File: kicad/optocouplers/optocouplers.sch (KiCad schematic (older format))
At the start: 112 parts, among them Q1 PN2222A, Q2 PN2222A, Q3 PN2222A, Q4 PN2222A, Q5 PN2222A, Q6 PN2222A, Q7 PN2222A, Q8 PN2222A

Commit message: update kicad drawings for optocouplers
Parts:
- added J1: Conn_02x13_Top_Bottom, symbol Conn_02x13_Top_Bottom
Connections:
- no-connect marks 0 -> 8

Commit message: Update to the latest version of optocoupler pcb design
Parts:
- J1: footprint (none) -> Connectors_Multicomp:Multicomp_MC9A12-2634_2x13x2.54mm_Straight; symbol Conn_02x13_Top_Bottom -> optocouplers-rescue:Conn_02x13_Top_Bottom
- Q1, Q2, Q3, Q4, Q5, Q6, Q7, Q8: symbol PN2222A -> optocouplers-rescue:PN2222A
- R1, R2, R3, R4, R5, R6, R7, R8, R_A0, R_A1, R_A10, R_A11, R_A2, R_A3, R_A4, R_A5, R_A6, R_A7, R_A8, R_A9, R_B0, R_B1, R_B10, R_B11, R_B12, R_B2, R_B3, R_B4, R_B5, R_B6, R_B7, R_B8, R_B9, R_C0, R_C1, R_C10, R_C11, R_C2, R_C3, R_C4, R_C5, R_C6, R_C7, R_C8, R_C9, R_D0, R_D1, R_D10, R_D2, R_D3, R_D4, R_D5, R_D6, R_D7, R_D8, R_D9: symbol R -> optocouplers-rescue:R
- U_A0, U_A1, U_A10, U_A11, U_A2, U_A3, U_A4, U_A5, U_A6, U_A7, U_A8, U_A9, U_B0, U_B1, U_B10, U_B11, U_B12, U_B2, U_B3, U_B4, U_B5, U_B6, U_B7, U_B8, U_B9, U_C0, U_C1, U_C10, U_C11, U_C2, U_C3, U_C4, U_C5, U_C6, U_C7, U_C8, U_C9, U_D0, U_D1, U_D10, U_D2, U_D3, U_D4, U_D5, U_D6, U_D7, U_D8, U_D9: symbol ITR9608 -> optocouplers-rescue:ITR9608
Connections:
- wire segments 56 -> 96

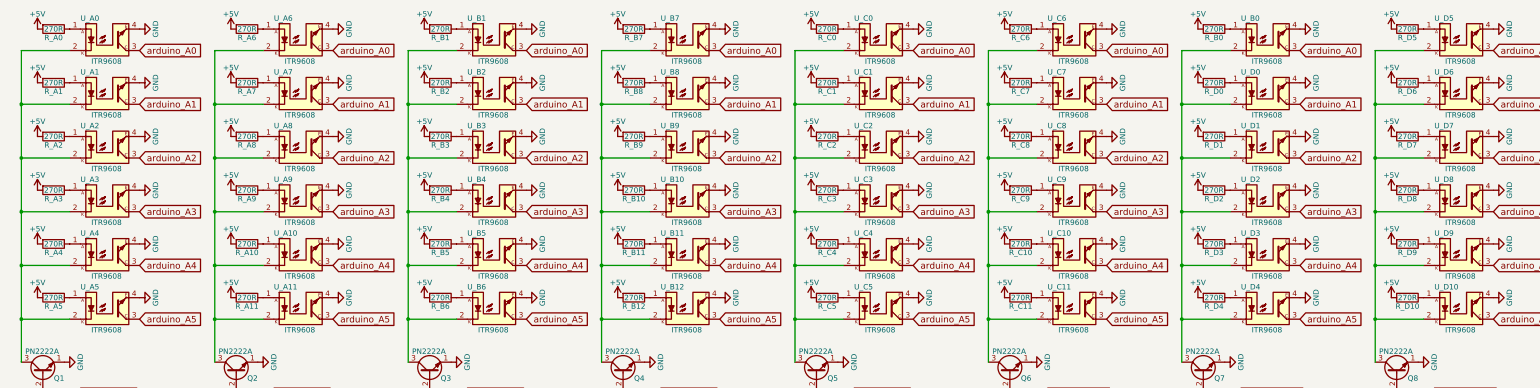
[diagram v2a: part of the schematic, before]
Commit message: Slightly change wiring of optocouplers
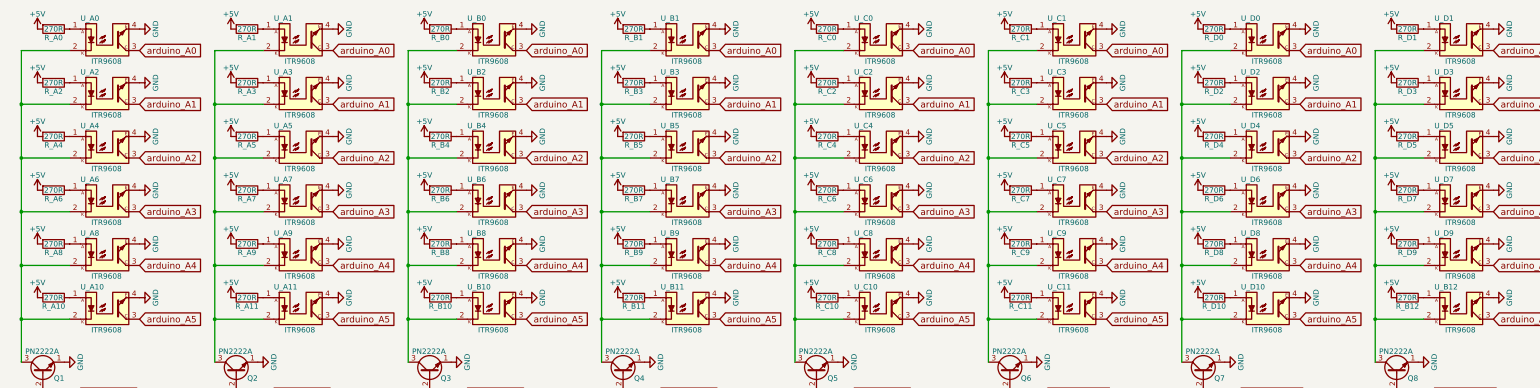
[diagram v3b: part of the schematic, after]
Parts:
- R1, R2, R3, R4, R5, R6, R7, R8, R_A0, R_A11, R_B2, R_C0, R_C11, R_D9: footprint Resistors_ThroughHole:R_Axial_DIN0207_L6.3mm_D2.5mm_P10.16mm_Horizontal -> Resistor_SMD:R_1206_3216Metric_Pad1.42x1.75mm_HandSolder
- R_A1: renamed from R_A6; footprint Resistors_ThroughHole:R_Axial_DIN0207_L6.3mm_D2.5mm_P10.16mm_Horizontal -> Resistor_SMD:R_1206_3216Metric_Pad1.42x1.75mm_HandSolder
- R_A10: renamed from R_A5; footprint Resistors_ThroughHole:R_Axial_DIN0207_L6.3mm_D2.5mm_P10.16mm_Horizontal -> Resistor_SMD:R_1206_3216Metric_Pad1.42x1.75mm_HandSolder
- R_A2: renamed from R_A1; footprint Resistors_ThroughHole:R_Axial_DIN0207_L6.3mm_D2.5mm_P10.16mm_Horizontal -> Resistor_SMD:R_1206_3216Metric_Pad1.42x1.75mm_HandSolder
- R_A3: renamed from R_A7; footprint Resistors_ThroughHole:R_Axial_DIN0207_L6.3mm_D2.5mm_P10.16mm_Horizontal -> Resistor_SMD:R_1206_3216Metric_Pad1.42x1.75mm_HandSolder
- R_A4: renamed from R_A2; footprint Resistors_ThroughHole:R_Axial_DIN0207_L6.3mm_D2.5mm_P10.16mm_Horizontal -> Resistor_SMD:R_1206_3216Metric_Pad1.42x1.75mm_HandSolder
- R_A5: renamed from R_A8; footprint Resistors_ThroughHole:R_Axial_DIN0207_L6.3mm_D2.5mm_P10.16mm_Horizontal -> Resistor_SMD:R_1206_3216Metric_Pad1.42x1.75mm_HandSolder
- R_A6: renamed from R_A3; footprint Resistors_ThroughHole:R_Axial_DIN0207_L6.3mm_D2.5mm_P10.16mm_Horizontal -> Resistor_SMD:R_1206_3216Metric_Pad1.42x1.75mm_HandSolder
- R_A7: renamed from R_A9; footprint Resistors_ThroughHole:R_Axial_DIN0207_L6.3mm_D2.5mm_P10.16mm_Horizontal -> Resistor_SMD:R_1206_3216Metric_Pad1.42x1.75mm_HandSolder
- R_A8: renamed from R_A4; footprint Resistors_ThroughHole:R_Axial_DIN0207_L6.3mm_D2.5mm_P10.16mm_Horizontal -> Resistor_SMD:R_1206_3216Metric_Pad1.42x1.75mm_HandSolder
- R_A9: renamed from R_A10; footprint Resistors_ThroughHole:R_Axial_DIN0207_L6.3mm_D2.5mm_P10.16mm_Horizontal -> Resistor_SMD:R_1206_3216Metric_Pad1.42x1.75mm_HandSolder
- R_B0: renamed from R_B1; footprint Resistors_ThroughHole:R_Axial_DIN0207_L6.3mm_D2.5mm_P10.16mm_Horizontal -> Resistor_SMD:R_1206_3216Metric_Pad1.42x1.75mm_HandSolder
- R_B1: renamed from R_B7; footprint Resistors_ThroughHole:R_Axial_DIN0207_L6.3mm_D2.5mm_P10.16mm_Horizontal -> Resistor_SMD:R_1206_3216Metric_Pad1.42x1.75mm_HandSolder
- R_B10: renamed from R_B6; footprint Resistors_ThroughHole:R_Axial_DIN0207_L6.3mm_D2.5mm_P10.16mm_Horizontal -> Resistor_SMD:R_1206_3216Metric_Pad1.42x1.75mm_HandSolder
- R_B11: renamed from R_B12; footprint Resistors_ThroughHole:R_Axial_DIN0207_L6.3mm_D2.5mm_P10.16mm_Horizontal -> Resistor_SMD:R_1206_3216Metric_Pad1.42x1.75mm_HandSolder
- R_B12: renamed from R_D10; footprint Resistors_ThroughHole:R_Axial_DIN0207_L6.3mm_D2.5mm_P10.16mm_Horizontal -> Resistor_SMD:R_1206_3216Metric_Pad1.42x1.75mm_HandSolder
- R_B3: renamed from R_B8; footprint Resistors_ThroughHole:R_Axial_DIN0207_L6.3mm_D2.5mm_P10.16mm_Horizontal -> Resistor_SMD:R_1206_3216Metric_Pad1.42x1.75mm_HandSolder
- R_B4: renamed from R_B3; footprint Resistors_ThroughHole:R_Axial_DIN0207_L6.3mm_D2.5mm_P10.16mm_Horizontal -> Resistor_SMD:R_1206_3216Metric_Pad1.42x1.75mm_HandSolder
- R_B5: renamed from R_B9; footprint Resistors_ThroughHole:R_Axial_DIN0207_L6.3mm_D2.5mm_P10.16mm_Horizontal -> Resistor_SMD:R_1206_3216Metric_Pad1.42x1.75mm_HandSolder
- R_B6: renamed from R_B4; footprint Resistors_ThroughHole:R_Axial_DIN0207_L6.3mm_D2.5mm_P10.16mm_Horizontal -> Resistor_SMD:R_1206_3216Metric_Pad1.42x1.75mm_HandSolder
- R_B7: renamed from R_B10; footprint Resistors_ThroughHole:R_Axial_DIN0207_L6.3mm_D2.5mm_P10.16mm_Horizontal -> Resistor_SMD:R_1206_3216Metric_Pad1.42x1.75mm_HandSolder
- R_B8: renamed from R_B5; footprint Resistors_ThroughHole:R_Axial_DIN0207_L6.3mm_D2.5mm_P10.16mm_Horizontal -> Resistor_SMD:R_1206_3216Metric_Pad1.42x1.75mm_HandSolder
- R_B9: renamed from R_B11; footprint Resistors_ThroughHole:R_Axial_DIN0207_L6.3mm_D2.5mm_P10.16mm_Horizontal -> Resistor_SMD:R_1206_3216Metric_Pad1.42x1.75mm_HandSolder
- R_C1: renamed from R_C6; footprint Resistors_ThroughHole:R_Axial_DIN0207_L6.3mm_D2.5mm_P10.16mm_Horizontal -> Resistor_SMD:R_1206_3216Metric_Pad1.42x1.75mm_HandSolder
- R_C10: renamed from R_C5; footprint Resistors_ThroughHole:R_Axial_DIN0207_L6.3mm_D2.5mm_P10.16mm_Horizontal -> Resistor_SMD:R_1206_3216Metric_Pad1.42x1.75mm_HandSolder
- R_C2: renamed from R_C1; footprint Resistors_ThroughHole:R_Axial_DIN0207_L6.3mm_D2.5mm_P10.16mm_Horizontal -> Resistor_SMD:R_1206_3216Metric_Pad1.42x1.75mm_HandSolder
- R_C3: renamed from R_C7; footprint Resistors_ThroughHole:R_Axial_DIN0207_L6.3mm_D2.5mm_P10.16mm_Horizontal -> Resistor_SMD:R_1206_3216Metric_Pad1.42x1.75mm_HandSolder
- R_C4: renamed from R_C2; footprint Resistors_ThroughHole:R_Axial_DIN0207_L6.3mm_D2.5mm_P10.16mm_Horizontal -> Resistor_SMD:R_1206_3216Metric_Pad1.42x1.75mm_HandSolder
- R_C5: renamed from R_C8; footprint Resistors_ThroughHole:R_Axial_DIN0207_L6.3mm_D2.5mm_P10.16mm_Horizontal -> Resistor_SMD:R_1206_3216Metric_Pad1.42x1.75mm_HandSolder
- R_C6: renamed from R_C3; footprint Resistors_ThroughHole:R_Axial_DIN0207_L6.3mm_D2.5mm_P10.16mm_Horizontal -> Resistor_SMD:R_1206_3216Metric_Pad1.42x1.75mm_HandSolder
- R_C7: renamed from R_C9; footprint Resistors_ThroughHole:R_Axial_DIN0207_L6.3mm_D2.5mm_P10.16mm_Horizontal -> Resistor_SMD:R_1206_3216Metric_Pad1.42x1.75mm_HandSolder
- R_C8: renamed from R_C4; footprint Resistors_ThroughHole:R_Axial_DIN0207_L6.3mm_D2.5mm_P10.16mm_Horizontal -> Resistor_SMD:R_1206_3216Metric_Pad1.42x1.75mm_HandSolder
- R_C9: renamed from R_C10; footprint Resistors_ThroughHole:R_Axial_DIN0207_L6.3mm_D2.5mm_P10.16mm_Horizontal -> Resistor_SMD:R_1206_3216Metric_Pad1.42x1.75mm_HandSolder
- R_D0: renamed from R_B0; footprint Resistors_ThroughHole:R_Axial_DIN0207_L6.3mm_D2.5mm_P10.16mm_Horizontal -> Resistor_SMD:R_1206_3216Metric_Pad1.42x1.75mm_HandSolder
- R_D1: renamed from R_D5; footprint Resistors_ThroughHole:R_Axial_DIN0207_L6.3mm_D2.5mm_P10.16mm_Horizontal -> Resistor_SMD:R_1206_3216Metric_Pad1.42x1.75mm_HandSolder
- R_D10: renamed from R_D4; footprint Resistors_ThroughHole:R_Axial_DIN0207_L6.3mm_D2.5mm_P10.16mm_Horizontal -> Resistor_SMD:R_1206_3216Metric_Pad1.42x1.75mm_HandSolder
- R_D2: renamed from R_D0; footprint Resistors_ThroughHole:R_Axial_DIN0207_L6.3mm_D2.5mm_P10.16mm_Horizontal -> Resistor_SMD:R_1206_3216Metric_Pad1.42x1.75mm_HandSolder
- R_D3: renamed from R_D6; footprint Resistors_ThroughHole:R_Axial_DIN0207_L6.3mm_D2.5mm_P10.16mm_Horizontal -> Resistor_SMD:R_1206_3216Metric_Pad1.42x1.75mm_HandSolder
- R_D4: renamed from R_D1; footprint Resistors_ThroughHole:R_Axial_DIN0207_L6.3mm_D2.5mm_P10.16mm_Horizontal -> Resistor_SMD:R_1206_3216Metric_Pad1.42x1.75mm_HandSolder
- R_D5: renamed from R_D7; footprint Resistors_ThroughHole:R_Axial_DIN0207_L6.3mm_D2.5mm_P10.16mm_Horizontal -> Resistor_SMD:R_1206_3216Metric_Pad1.42x1.75mm_HandSolder
- R_D6: renamed from R_D2; footprint Resistors_ThroughHole:R_Axial_DIN0207_L6.3mm_D2.5mm_P10.16mm_Horizontal -> Resistor_SMD:R_1206_3216Metric_Pad1.42x1.75mm_HandSolder
- R_D7: renamed from R_D8; footprint Resistors_ThroughHole:R_Axial_DIN0207_L6.3mm_D2.5mm_P10.16mm_Horizontal -> Resistor_SMD:R_1206_3216Metric_Pad1.42x1.75mm_HandSolder
- R_D8: renamed from R_D3; footprint Resistors_ThroughHole:R_Axial_DIN0207_L6.3mm_D2.5mm_P10.16mm_Horizontal -> Resistor_SMD:R_1206_3216Metric_Pad1.42x1.75mm_HandSolder
- renumbered U_A6 to U_A1, U_A5 to U_A10, U_A1 to U_A2, U_A7 to U_A3, U_A2 to U_A4, U_A8 to U_A5, U_A3 to U_A6, U_A9 to U_A7, U_A4 to U_A8, U_A10 to U_A9, U_B1 to U_B0, U_B7 to U_B1, U_B6 to U_B10, U_B12 to U_B11, U_D10 to U_B12, U_B8 to U_B3, U_B3 to U_B4, U_B9 to U_B5, U_B4 to U_B6, U_B10 to U_B7, U_B5 to U_B8, U_B11 to U_B9, U_C6 to U_C1, U_C5 to U_C10, U_C1 to U_C2, U_C7 to U_C3, U_C2 to U_C4, U_C8 to U_C5, U_C3 to U_C6, U_C9 to U_C7, U_C4 to U_C8, U_C10 to U_C9, U_B0 to U_D0, U_D5 to U_D1, U_D4 to U_D10, U_D0 to U_D2, U_D6 to U_D3, U_D1 to U_D4, U_D7 to U_D5, U_D2 to U_D6, U_D8 to U_D7, U_D3 to U_D8

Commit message: almost complete pcb
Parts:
- removed J1: Conn_02x13_Top_Bottom, Connectors_Multicomp:Multicomp_MC9A12-2634_2x13x2.54mm_Straight, symbol optocouplers-rescue:Conn_02x13_Top_Bottom
- added Conn1: Conn_02x13_Odd_Even, Connector_Multicomp:Multicomp_MC9A12-2634_2x13_P2.54mm_Vertical, symbol Connector_Generic:Conn_02x13_Odd_Even
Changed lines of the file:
@@
-$EndComp
-$Comp
-L optocouplers-rescue:Conn_02x13_Top_Bottom J1
-U 1 1 5A4545DE
-P 2900 5600
-F 0 "J1" H 2950 6417 50  0000 C CNN
-F 1 "Conn_02x13_Top_Bottom" H 2950 6326 50  0000 C CNN
-F 2 "Connectors_Multicomp:Multicomp_MC9A12-2634_2x13x2.54mm_Straight" H 2900 5600 50  0001 C CNN
-F 3 "~" H 2900 5600 50  0001 C CNN
-	1    2900 5600
-	1    0    0    -1
 $EndComp
 $Comp
@@
 L optocouplers-rescue:GND #PWR0109
 U 1 1 5A4568BF
-P 3200 5100
-F 0 "#PWR0109" H 3200 4850 50  0001 C CNN
-F 1 "GND" V 3205 4972 50  0000 R CNN
-F 2 "" H 3200 5100 50  0001 C CNN
-F 3 "" H 3200 5100 50  0001 C CNN
-	1    3200 5100
+P 3200 6200
+F 0 "#PWR0109" H 3200 5950 50  0001 C CNN
+F 1 "GND" V 3205 6072 50  0000 R CNN
+F 2 "" H 3200 6200 50  0001 C CNN
+F 3 "" H 3200 6200 50  0001 C CNN
+	1    3200 6200
 	0    -1   -1   0
 $EndComp
@@
 L optocouplers-rescue:GND #PWR0110
 U 1 1 5A456B8E
-P 2700 5100
-F 0 "#PWR0110" H 2700 4850 50  0001 C CNN
-F 1 "GND" V 2705 4972 50  0000 R CNN
-F 2 "" H 2700 5100 50  0001 C CNN
-F 3 "" H 2700 5100 50  0001 C CNN
-	1    2700 5100
+P 2700 6200
+F 0 "#PWR0110" H 2700 5950 50  0001 C CNN
+F 1 "GND" V 2705 6072 50  0000 R CNN
+F 2 "" H 2700 6200 50  0001 C CNN
+F 3 "" H 2700 6200 50  0001 C CNN
+	1    2700 6200
 	0    1    1    0
 $EndComp
-Text GLabel 2700 6200 0    60   Input ~ 0
+Text GLabel 2700 5800 0    60   Input ~ 0
 arduino_D12
-Text GLabel 2700 6100 0    60   Input ~ 0
+Text GLabel 2700 5700 0    60   Input ~ 0
 arduino_D11
-Text GLabel 2700 6000 0    60   Input ~ 0
+Text GLabel 2700 5600 0    60   Input ~ 0
 arduino_D10
-Text GLabel 2700 5900 0    60   Input ~ 0
+Text GLabel 2700 5500 0    60   Input ~ 0
 arduino_D9
-Text GLabel 2700 5800 0    60   Input ~ 0
+Text GLabel 2700 5400 0    60   Input ~ 0
 arduino_D8
-Text GLabel 2700 5700 0    60   Input ~ 0
+Text GLabel 2700 5300 0    60   Input ~ 0
 arduino_D7
-Text GLabel 2700 5600 0    60   Input ~ 0
+Text GLabel 2700 5200 0    60   Input ~ 0
 arduino_D6
-Text GLabel 2700 5500 0    60   Input ~ 0
+Text GLabel 2700 5100 0    60   Input ~ 0
 arduino_D5
-NoConn ~ 2700 5400
-NoConn ~ 2700 5300
-NoConn ~ 2700 5200
+Text GLabel 3200 5100 2    60   Input ~ 0
+arduino_A5
+Text GLabel 3200 5200 2    60   Input ~ 0
+arduino_A4
+Text GLabel 3200 5300 2    60   Input ~ 0
+arduino_A3
 Text GLabel 3200 5400 2    60   Input ~ 0
-arduino_A5
+arduino_A2
 Text GLabel 3200 5500 2    60   Input ~ 0
-arduino_A4
+arduino_A1
 Text GLabel 3200 5600 2    60   Input ~ 0
-arduino_A3
-Text GLabel 3200 5700 2    60   Input ~ 0
-arduino_A2
-Text GLabel 3200 5800 2    60   Input ~ 0
-arduino_A1
-Text GLabel 3200 5900 2    60   Input ~ 0
 arduino_A0
-NoConn ~ 3200 6200
 NoConn ~ 3200 6100
 NoConn ~ 3200 6000
-NoConn ~ 3200 5300
-NoConn ~ 3200 5200
 Wire Wire Line
 	900  2200 900  2700
@@
 Wire Wire Line
 	900  1700 900  2200
+NoConn ~ 2700 5900
+NoConn ~ 2700 6000
+NoConn ~ 2700 6100
+NoConn ~ 3200 5700
+NoConn ~ 3200 5800
+NoConn ~ 3200 5900
+$Comp
+L Connector_Generic:Conn_02x13_Odd_Even Conn1
+U 1 1 5D7EB063
+P 2900 5600
+F 0 "Conn1" H 2950 6417 50  0000 C CNN
+F 1 "Conn_02x13_Odd_Even" H 2950 6326 50  0000 C CNN
+F 2 "Connector_Multicomp:Multicomp_MC9A12-2634_2x13_P2.54mm_Vertical" H 2900 5600 50  0001 C CNN
+F 3 "~" H 2900 5600 50  0001 C CNN
+	1    2900 5600
+	1    0    0    -1
+$EndComp
 $EndSCHEMATC

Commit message: Add missing 2k resistors, change connectors (opto)
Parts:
- added R_R0, R_R1, R_R2, R_R3, R_R4, R_R5: 2k, symbol Device:R
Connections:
- net +5V: now also R_R0.2, R_R1.2, R_R2.2, R_R3.2, R_R4.2, R_R5.2
- net arduino_A0: now also R_R0.1
- net arduino_A1: now also R_R1.1
- net arduino_A2: now also R_R2.1
- net arduino_A3: now also R_R3.1
- net arduino_A4: now also R_R4.1
- net arduino_A5: now also R_R5.1
- net arduino_D10: now also Conn1.19 (Pin_19); no longer Conn1.13 (Pin_13)
- net arduino_D11: now also Conn1.21 (Pin_21); no longer Conn1.15 (Pin_15)
- net arduino_D12: now also Conn1.23 (Pin_23); no longer Conn1.17 (Pin_17)
- net arduino_D5: now also Conn1.9 (Pin_9); no longer Conn1.3 (Pin_3)
- net arduino_D6: now also Conn1.11 (Pin_11); no longer Conn1.5 (Pin_5)
- net arduino_D7: now also Conn1.13 (Pin_13); no longer Conn1.7 (Pin_7)
- net arduino_D8: now also Conn1.15 (Pin_15); no longer Conn1.9 (Pin_9)
- net arduino_D9: now also Conn1.17 (Pin_17); no longer Conn1.11 (Pin_11)
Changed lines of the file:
@@
 EESchema Schematic File Version 4
 LIBS:optocouplers-cache
-EELAYER 26 0
+EELAYER 30 0
 EELAYER END
 $Descr User 17717 7087
@@
 	0    1    1    0
 $EndComp
+Text GLabel 2700 6100 0    60   Input ~ 0
+arduino_D12
+Text GLabel 2700 6000 0    60   Input ~ 0
+arduino_D11
+Text GLabel 2700 5900 0    60   Input ~ 0
+arduino_D10
 Text GLabel 2700 5800 0    60   Input ~ 0
-arduino_D12
+arduino_D9
 Text GLabel 2700 5700 0    60   Input ~ 0
-arduino_D11
+arduino_D8
 Text GLabel 2700 5600 0    60   Input ~ 0
-arduino_D10
+arduino_D7
 Text GLabel 2700 5500 0    60   Input ~ 0
-arduino_D9
+arduino_D6
 Text GLabel 2700 5400 0    60   Input ~ 0
-arduino_D8
-Text GLabel 2700 5300 0    60   Input ~ 0
-arduino_D7
-Text GLabel 2700 5200 0    60   Input ~ 0
-arduino_D6
-Text GLabel 2700 5100 0    60   Input ~ 0
 arduino_D5
 Text GLabel 3200 5100 2    60   Input ~ 0
@@
 Wire Wire Line
 	900  1700 900  2200
-NoConn ~ 2700 5900
-NoConn ~ 2700 6000
-NoConn ~ 2700 6100
 NoConn ~ 3200 5700
 NoConn ~ 3200 5800
@@
 	1    0    0    -1
 $EndComp
+Text GLabel 15600 1700 2    60   Input ~ 0
+arduino_A1
+Text GLabel 15600 1200 2    60   Input ~ 0
+arduino_A0
+Text GLabel 15600 2700 2    60   Input ~ 0
+arduino_A3
+Text GLabel 15600 2200 2    60   Input ~ 0
+arduino_A2
+Text GLabel 15600 3700 2    60   Input ~ 0
+arduino_A5
+Text GLabel 15600 3200 2    60   Input ~ 0
+arduino_A4
+$Comp
+L power:+5V #PWR0111
+U 1 1 5DB2BCC0
+P 15300 1200
+F 0 "#PWR0111" H 15300 1050 50  0001 C CNN
+F 1 "+5V" H 15315 1373 50  0000 C CNN
+F 2 "" H 15300 1200 50  0001 C CNN
+F 3 "" H 15300 1200 50  0001 C CNN
+	1    15300 1200
+	1    0    0    -1
+$EndComp
+$Comp
+L power:+5V #PWR0112
+U 1 1 5DB2C8AB
+P 15300 1700
+F 0 "#PWR0112" H 15300 1550 50  0001 C CNN
+F 1 "+5V" H 15315 1873 50  0000 C CNN
+F 2 "" H 15300 1700 50  0001 C CNN
+F 3 "" H 15300 1700 50  0001 C CNN
+	1    15300 1700
+	1    0    0    -1
+$EndComp
+$Comp
+L Device:R R_R2
+U 1 1 5DB2ED55
+P 15450 2200
+F 0 "R_R2" V 15550 2200 50  0000 C CNN
+F 1 "2k" V 15450 2200 50  0000 C CNN
+F 2 "" V 15380 2200 50  0001 C CNN
+F 3 "~" H 15450 2200 50  0001 C CNN
+	1    15450 2200
+	0    1    1    0
+$EndComp
+$Comp
+L power:+5V #PWR0113
+U 1 1 5DB2ED5B
+P 15300 2200
+F 0 "#PWR0113" H 15300 2050 50  0001 C CNN
+F 1 "+5V" H 15315 2373 50  0000 C CNN
+F 2 "" H 15300 2200 50  0001 C CNN
+F 3 "" H 15300 2200 50  0001 C CNN
+	1    15300 2200
+	1    0    0    -1
+$EndComp
+$Comp
+L Device:R R_R3
+U 1 1 5DB31435
+P 15450 2700
+F 0 "R_R3" V 15550 2700 50  0000 C CNN
+F 1 "2k" V 15450 2700 50  0000 C CNN
+F 2 "" V 15380 2700 50  0001 C CNN
+F 3 "~" H 15450 2700 50  0001 C CNN
+	1    15450 2700
+	0    1    1    0
+$EndComp
+$Comp
+L power:+5V #PWR0114
+U 1 1 5DB3143B
+P 15300 2700
+F 0 "#PWR0114" H 15300 2550 50  0001 C CNN
+F 1 "+5V" H 15315 2873 50  0000 C CNN
+F 2 "" H 15300 2700 50  0001 C CNN
+F 3 "" H 15300 2700 50  0001 C CNN
+	1    15300 2700
+	1    0    0    -1
+$EndComp
+$Comp
+L Device:R R_R4
+U 1 1 5DB3377D
+P 15450 3200
+F 0 "R_R4" V 15550 3200 50  0000 C CNN
+F 1 "2k" V 15450 3200 50  0000 C CNN
+F 2 "" V 15380 3200 50  0001 C CNN
+F 3 "~" H 15450 3200 50  0001 C CNN
+	1    15450 3200
+	0    1    1    0
+$EndComp
+$Comp
+L power:+5V #PWR0115
+U 1 1 5DB33783
+P 15300 3200
+F 0 "#PWR0115" H 15300 3050 50  0001 C CNN
+F 1 "+5V" H 15315 3373 50  0000 C CNN
+F 2 "" H 15300 3200 50  0001 C CNN
+F 3 "" H 15300 3200 50  0001 C CNN
+	1    15300 3200
+	1    0    0    -1
+$EndComp
+$Comp
+L Device:R R_R5
+U 1 1 5DB35C7D
+P 15450 3700
+F 0 "R_R5" V 15550 3700 50  0000 C CNN
+F 1 "2k" V 15450 3700 50  0000 C CNN
+F 2 "" V 15380 3700 50  0001 C CNN
+F 3 "~" H 15450 3700 50  0001 C CNN
+	1    15450 3700
+	0    1    1    0
+$EndComp
+$Comp
+L power:+5V #PWR0116
+U 1 1 5DB35C83
+P 15300 3700
+F 0 "#PWR0116" H 15300 3550 50  0001 C CNN
+F 1 "+5V" H 15315 3873 50  0000 C CNN
+F 2 "" H 15300 3700 50  0001 C CNN
+F 3 "" H 15300 3700 50  0001 C CNN
+	1    15300 3700
+	1    0    0    -1
+$EndComp
+NoConn ~ 2700 5300
+NoConn ~ 2700 5200
+$Comp
+L Device:R R_R0
+U 1 1 5DB27A45
+P 15450 1200
+F 0 "R_R0" V 15550 1200 50  0000 C CNN
+F 1 "2k" V 15450 1200 50  0000 C CNN
+F 2 "" V 15380 1200 50  0001 C CNN
+F 3 "~" H 15450 1200 50  0001 C CNN
+	1    15450 1200
+	0    1    1    0
+$EndComp
+$Comp
+L Device:R R_R1
+U 1 1 5DB2C8A5
+P 15450 1700
+F 0 "R_R1" V 15550 1700 50  0000 C CNN
+F 1 "2k" V 15450 1700 50  0000 C CNN
+F 2 "" V 15380 1700 50  0001 C CNN
+F 3 "~" H 15450 1700 50  0001 C CNN
+	1    15450 1700
+	0    1    1    0
+$EndComp
+NoConn ~ 2700 5100
 $EndSCHEMATC

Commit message: Assign correct footprint of transistors, missing resistors
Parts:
- Q1, Q2, Q3, Q4, Q5, Q6, Q7, Q8: footprint TO_SOT_Packages_THT:TO-92_Molded_Narrow -> Package_TO_SOT_THT:TO-92_Inline
- R_R0, R_R1, R_R2, R_R3, R_R4, R_R5: footprint (none) -> Resistor_SMD:R_1206_3216Metric_Pad1.42x1.75mm_HandSolder
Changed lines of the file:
@@
 F 0 "Q1" V 1050 4000 50  0000 L CNN
 F 1 "PN2222A" V 1300 4050 50  0000 L CNN
-F 2 "TO_SOT_Packages_THT:TO-92_Molded_Narrow" H 1300 4125 50  0001 L CIN
+F 2 "Package_TO_SOT_THT:TO-92_Inline" H 1300 4125 50  0001 L CIN
 F 3 "" H 1100 4200 50  0001 L CNN
 	1    1100 4200
@@
 F 0 "Q2" V 2850 4000 50  0000 L CNN
 F 1 "PN2222A" V 3100 4050 50  0000 L CNN
-F 2 "TO_SOT_Packages_THT:TO-92_Molded_Narrow" H 3100 4125 50  0001 L CIN
+F 2 "Package_TO_SOT_THT:TO-92_Inline" H 3100 4125 50  0001 L CIN
 F 3 "" H 2900 4200 50  0001 L CNN
 	1    2900 4200
@@
 F 0 "Q3" V 4650 4000 50  0000 L CNN
 F 1 "PN2222A" V 4900 4050 50  0000 L CNN
-F 2 "TO_SOT_Packages_THT:TO-92_Molded_Narrow" H 4900 4125 50  0001 L CIN
+F 2 "Package_TO_SOT_THT:TO-92_Inline" H 4900 4125 50  0001 L CIN
 F 3 "" H 4700 4200 50  0001 L CNN
 	1    4700 4200
@@
 F 0 "Q4" V 6450 4000 50  0000 L CNN
 F 1 "PN2222A" V 6700 4050 50  0000 L CNN
-F 2 "TO_SOT_Packages_THT:TO-92_Molded_Narrow" H 6700 4125 50  0001 L CIN
+F 2 "Package_TO_SOT_THT:TO-92_Inline" H 6700 4125 50  0001 L CIN
 F 3 "" H 6500 4200 50  0001 L CNN
 	1    6500 4200
@@
 F 0 "Q5" V 8250 4000 50  0000 L CNN
 F 1 "PN2222A" V 8500 4050 50  0000 L CNN
-F 2 "TO_SOT_Packages_THT:TO-92_Molded_Narrow" H 8500 4125 50  0001 L CIN
+F 2 "Package_TO_SOT_THT:TO-92_Inline" H 8500 4125 50  0001 L CIN
 F 3 "" H 8300 4200 50  0001 L CNN
 	1    8300 4200
@@
 F 0 "Q6" V 10050 4000 50  0000 L CNN
 F 1 "PN2222A" V 10300 4050 50  0000 L CNN
-F 2 "TO_SOT_Packages_THT:TO-92_Molded_Narrow" H 10300 4125 50  0001 L CIN
+F 2 "Package_TO_SOT_THT:TO-92_Inline" H 10300 4125 50  0001 L CIN
 F 3 "" H 10100 4200 50  0001 L CNN
 	1    10100 4200
@@
 F 0 "Q7" V 11850 4000 50  0000 L CNN
 F 1 "PN2222A" V 12100 4050 50  0000 L CNN
-F 2 "TO_SOT_Packages_THT:TO-92_Molded_Narrow" H 12100 4125 50  0001 L CIN
+F 2 "Package_TO_SOT_THT:TO-92_Inline" H 12100 4125 50  0001 L CIN
 F 3 "" H 11900 4200 50  0001 L CNN
 	1    11900 4200
@@
 F 0 "Q8" V 13650 4000 50  0000 L CNN
 F 1 "PN2222A" V 13900 4050 50  0000 L CNN
-F 2 "TO_SOT_Packages_THT:TO-92_Molded_Narrow" H 13900 4125 50  0001 L CIN
+F 2 "Package_TO_SOT_THT:TO-92_Inline" H 13900 4125 50  0001 L CIN
 F 3 "" H 13700 4200 50  0001 L CNN
 	1    13700 4200
@@
 F 0 "R_R2" V 15550 2200 50  0000 C CNN
 F 1 "2k" V 15450 2200 50  0000 C CNN
-F 2 "" V 15380 2200 50  0001 C CNN
+F 2 "Resistor_SMD:R_1206_3216Metric_Pad1.42x1.75mm_HandSolder" V 15380 2200 50  0001 C CNN
 F 3 "~" H 15450 2200 50  0001 C CNN
 	1    15450 2200
@@
 F 0 "R_R3" V 15550 2700 50  0000 C CNN
 F 1 "2k" V 15450 2700 50  0000 C CNN
-F 2 "" V 15380 2700 50  0001 C CNN
+F 2 "Resistor_SMD:R_1206_3216Metric_Pad1.42x1.75mm_HandSolder" V 15380 2700 50  0001 C CNN
 F 3 "~" H 15450 2700 50  0001 C CNN
 	1    15450 2700
@@
 F 0 "R_R4" V 15550 3200 50  0000 C CNN
 F 1 "2k" V 15450 3200 50  0000 C CNN
-F 2 "" V 15380 3200 50  0001 C CNN
+F 2 "Resistor_SMD:R_1206_3216Metric_Pad1.42x1.75mm_HandSolder" V 15380 3200 50  0001 C CNN
 F 3 "~" H 15450 3200 50  0001 C CNN
 	1    15450 3200
@@
 F 0 "R_R5" V 15550 3700 50  0000 C CNN
 F 1 "2k" V 15450 3700 50  0000 C CNN
-F 2 "" V 15380 3700 50  0001 C CNN
+F 2 "Resistor_SMD:R_1206_3216Metric_Pad1.42x1.75mm_HandSolder" V 15380 3700 50  0001 C CNN
 F 3 "~" H 15450 3700 50  0001 C CNN
 	1    15450 3700
@@
 F 0 "R_R0" V 15550 1200 50  0000 C CNN
 F 1 "2k" V 15450 1200 50  0000 C CNN
-F 2 "" V 15380 1200 50  0001 C CNN
+F 2 "Resistor_SMD:R_1206_3216Metric_Pad1.42x1.75mm_HandSolder" V 15380 1200 50  0001 C CNN
 F 3 "~" H 15450 1200 50  0001 C CNN
 	1    15450 1200
@@
 F 0 "R_R1" V 15550 1700 50  0000 C CNN
 F 1 "2k" V 15450 1700 50  0000 C CNN
-F 2 "" V 15380 1700 50  0001 C CNN
+F 2 "Resistor_SMD:R_1206_3216Metric_Pad1.42x1.75mm_HandSolder" V 15380 1700 50  0001 C CNN
 F 3 "~" H 15450 1700 50  0001 C CNN
 	1    15450 1700
